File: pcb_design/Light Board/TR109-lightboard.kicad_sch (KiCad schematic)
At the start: 11 parts, among them J1 Conn_01x05_Female

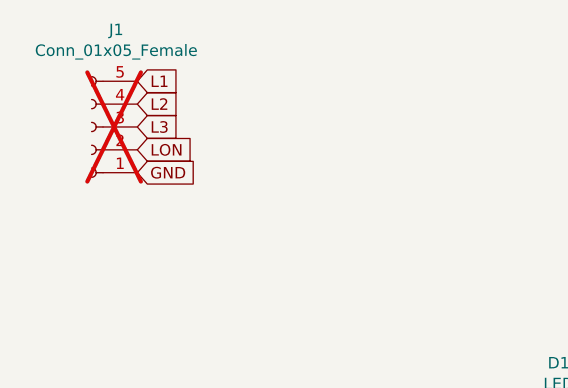
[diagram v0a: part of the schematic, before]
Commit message: Fixed some kicad PCB errors, updated Blender file
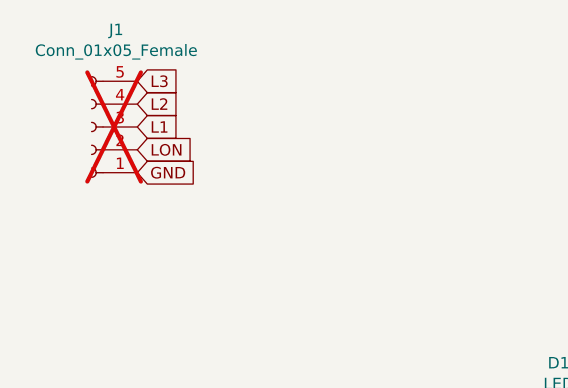
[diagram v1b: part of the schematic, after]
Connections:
- net L1: now also J1.3 (Pin_3); no longer J1.5 (Pin_5)
- net L3: now also J1.5 (Pin_5); no longer J1.3 (Pin_3)
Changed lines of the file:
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@@
 	(global_label "L3"
 		(shape input)
-		(at 77.47 78.74 0)
+		(at 77.47 73.66 0)
 		(effects
 			(font
@@
 		)
 		(property "Intersheetrefs" "${INTERSHEET_REFS}"
-			(at 77.47 78.74 0)
+			(at 77.47 73.66 0)
 			(effects
 				(font
@@
 	(global_label "L1"
 		(shape input)
-		(at 77.47 73.66 0)
+		(at 77.47 78.74 0)
 		(effects
 			(font
@@
 		)
 		(property "Intersheetrefs" "${INTERSHEET_REFS}"
-			(at 77.47 73.66 0)
+			(at 77.47 78.74 0)
 			(effects
 				(font
